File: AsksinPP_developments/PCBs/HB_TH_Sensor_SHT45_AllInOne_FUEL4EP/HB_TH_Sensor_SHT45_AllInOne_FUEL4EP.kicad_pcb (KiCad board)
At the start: 2 copper layers, 25 x 75 mm, 41 parts, among them J1 Conn_01x03, J2 FTDI Debuger, J3 ISP Programmer, SW1 Config button, U1 ATmega1284P-AU, U2 TPS61221DCK, U3 SHT45-AD1B-R2

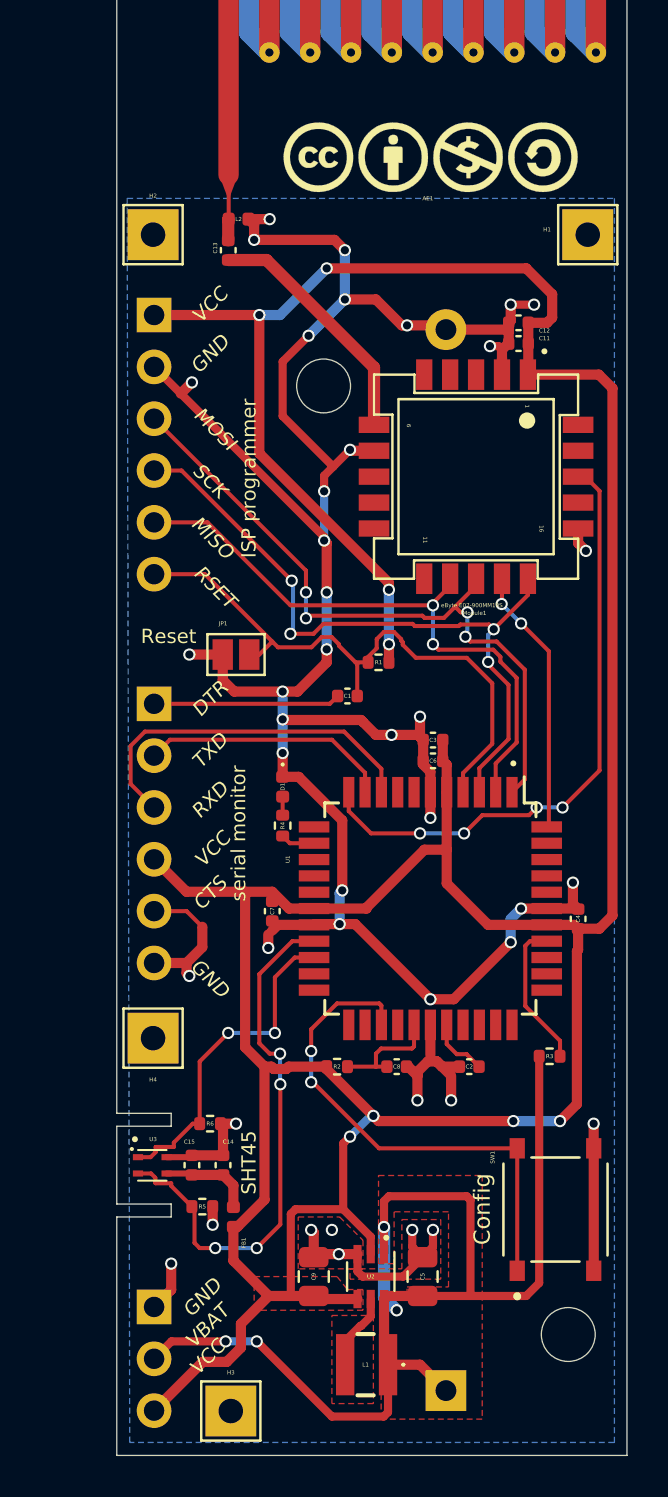
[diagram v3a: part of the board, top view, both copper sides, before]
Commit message: PCBs: updates of HB_TH_Sensor_SHT45_AllInOne_FUEL4EP and HB_Stamp_ATMega1284P_FUEL4EP see README.mds
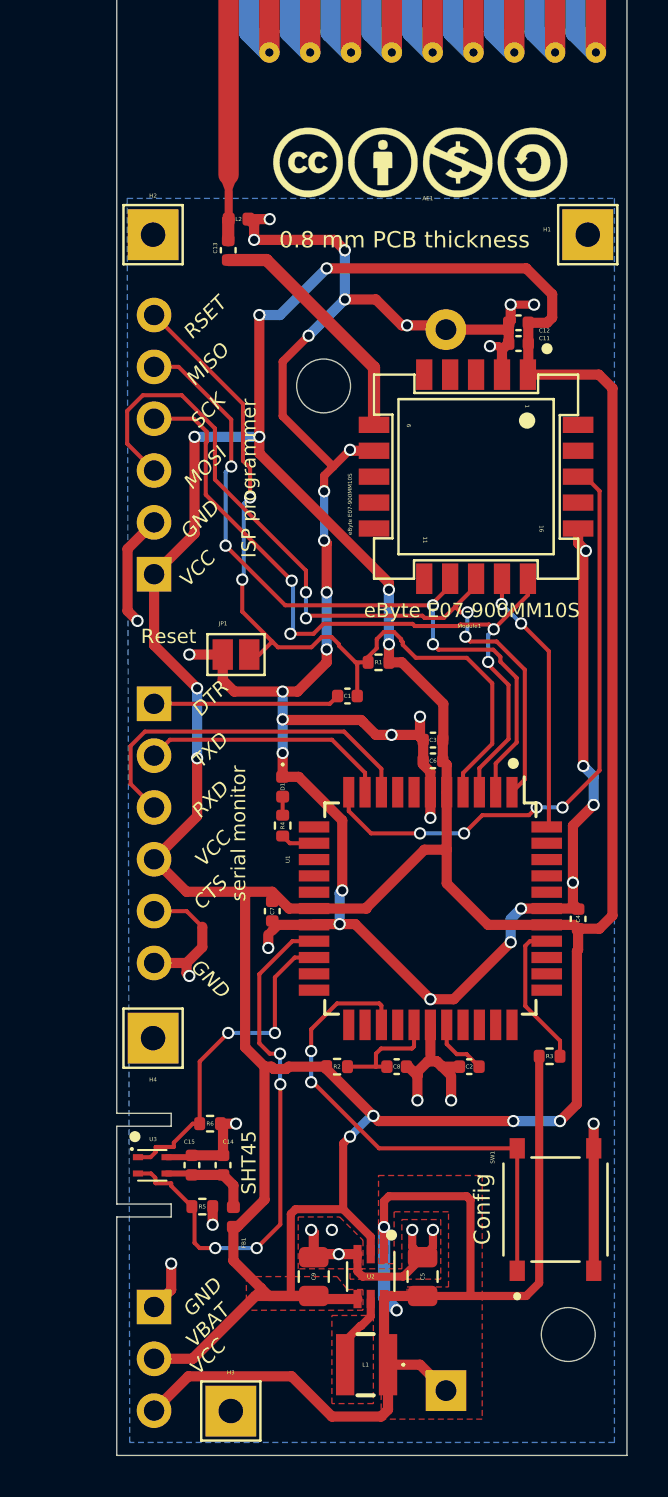
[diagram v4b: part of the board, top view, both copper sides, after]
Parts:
- moved J3 12.7 mm to (1.83, -43.2), turned to 0 degrees
- moved LOGO1 0.57 mm to (14.9, -63.4)
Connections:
- J1 pad 2: /plusBAT -> VCC
- J1 pad 3: VCC -> /plusBAT
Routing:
- net VCC: track 183.6 -> 215.4 mm, vias 8 -> 12
- net /RSETB: track 30.3 -> 41.8 mm, vias 0 -> 2
- net GND: track 153.9 -> 163.6 mm, vias 42 -> 44
- net /MISO: track 29.4 -> 36.6 mm, vias 2 -> 4
- net /MOSI: track 33.7 -> 40.8 mm
- net /SCK: track 34.3 -> 37.2 mm
- net /plusBAT: track 57.2 -> 56.8 mm, vias 4 -> 2
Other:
- board text added: "0.8 mm PCB thickness"
- board text added: "868 MHz SWRA416 antenna"
- board text added: "BAT"
- board text added: "RESETB"
- board text added: "RXD0"
- board text added: "TXD0"
- board text added: "Version 1.3 - 01/2024 (KiCAD 6)"
- board text added: "eByte E07-900MM10S"
- board text removed: "Version 1.2 - 01/2024 (KiCAD 6)"

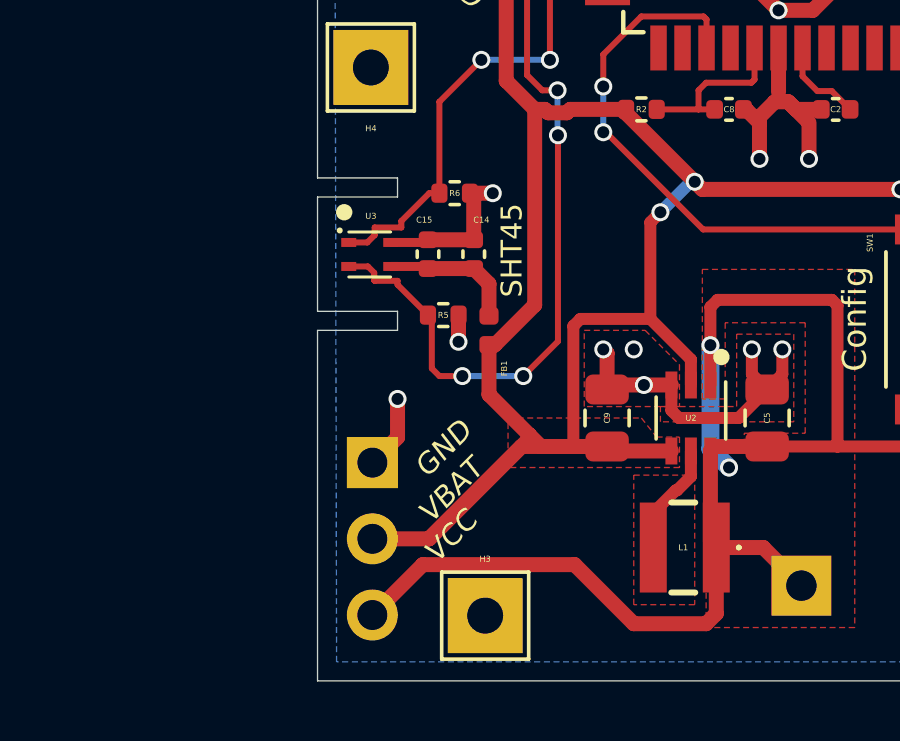
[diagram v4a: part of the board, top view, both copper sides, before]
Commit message: PCBs: fix of I2C Pull-up resistors that were wrongly tied to GND
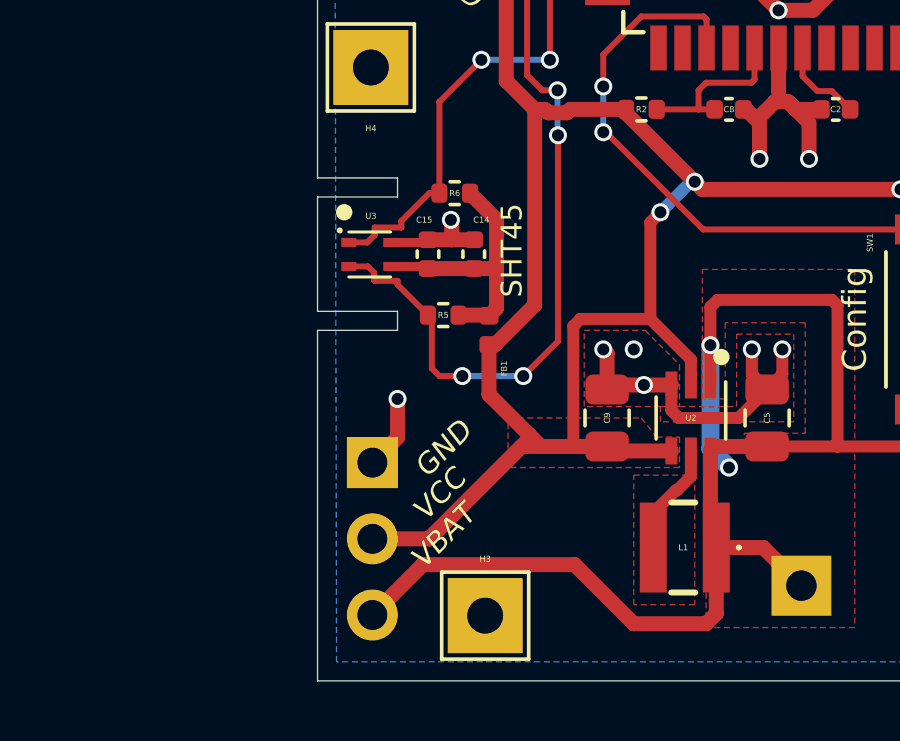
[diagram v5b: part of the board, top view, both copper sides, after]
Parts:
- turned R5 to 180 degrees
- turned R6 to 180 degrees
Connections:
- R5 pad 1: /SCL -> /VDDA
- R5 pad 2: GND -> /SCL
- R6 pad 1: /SDA -> /VDDA
- R6 pad 2: GND -> /SDA
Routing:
- net /VDDA: track 4.48 -> 9.08 mm
- net GND: track 163.6 -> 161.1 mm, vias 44 -> 43
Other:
- board text added: "Version 1.4 - 02/2024 (KiCAD 6)"
- board text removed: "Version 1.3 - 01/2024 (KiCAD 6)"
